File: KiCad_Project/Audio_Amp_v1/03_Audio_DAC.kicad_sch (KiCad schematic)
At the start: 0 parts

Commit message: Updated Power management section, Bluetooth receiver and connectors. Added some components footprints and 3D.
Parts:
- added U1: PCM2704CDB, PCM2704CDB:SOP65P780X200-28N, symbol PCM2704CDB:PCM2704CDB
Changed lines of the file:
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@@
 	(generator_version "9.0")
 	(paper "A4")
+	(symbol
+		(lib_id "PCM2704CDB:PCM2704CDB")
+		(at 134.62 97.79 0)
+		(unit 1)
+		(exclude_from_sim no)
+		(in_bom yes)
+		(on_board yes)
+		(dnp no)
+		(fields_autoplaced yes)
+		(property "Reference" "U1"
+			(at 134.62 57.15 0)
+			(effects
+				(font
+					(size 1.27 1.27)
+				)
+			)
+		)
+		(property "Value" "PCM2704CDB"
+			(at 134.62 59.69 0)
+			(effects
+				(font
+					(size 1.27 1.27)
+				)
+			)
+		)
+		(property "Footprint" "PCM2704CDB:SOP65P780X200-28N"
+			(at 134.62 97.79 0)
+			(effects
+				(font
+					(size 1.27 1.27)
+				)
+				(justify bottom)
+				(hide yes)
+			)
+		)
+		(property "Datasheet" "kicad-embed://pcm2704c.pdf"
+			(at 134.62 97.79 0)
+			(effects
+				(font
+					(size 1.27 1.27)
+				)
+				(hide yes)
+			)
+		)
+		(property "Description" "IC DAS/ADC/DAC SPECIAL 28-SSOP"
+			(at 134.62 97.79 0)
+			(effects
+				(font
+					(size 1.27 1.27)
+				)
+				(hide yes)
+			)
+		)
+		(pin "28"
+		)
+		(pin "4"
+		)
+		(pin "3"
+		)
+		(pin "21"
+		)
+		(pin "18"
+		)
+		(pin "23"
+		)
+		(pin "5"
+		)
+		(pin "7"
+		)
+		(pin "10"
+		)
+		(pin "20"
+		)
+		(pin "26"
+		)
+		(pin "22"
+		)
+		(pin "14"
+		)
+		(pin "15"
+		)
+		(pin "11"
+		)
+		(pin "24"
+		)
+		(pin "9"
+		)
+		(pin "25"
+		)
+		(pin "8"
+		)
+		(pin "13"
+		)
+		(pin "16"
+		)
+		(pin "27"
+		)
+		(pin "6"
+		)
+		(pin "1"
+		)
+		(pin "2"
+		)
+		(pin "12"
+		)
+		(pin "17"
+		)
+		(pin "19"
+		)
+		(instances
+			(project ""
+				(path "/d992164b-b1d0-4285-be2c-12a40c17e5cc/b3acd54a-fc58-4bfe-bc83-94fecc26a81e"
+					(reference "U1")
+					(unit 1)
+				)
+			)
+		)
+	)
 )

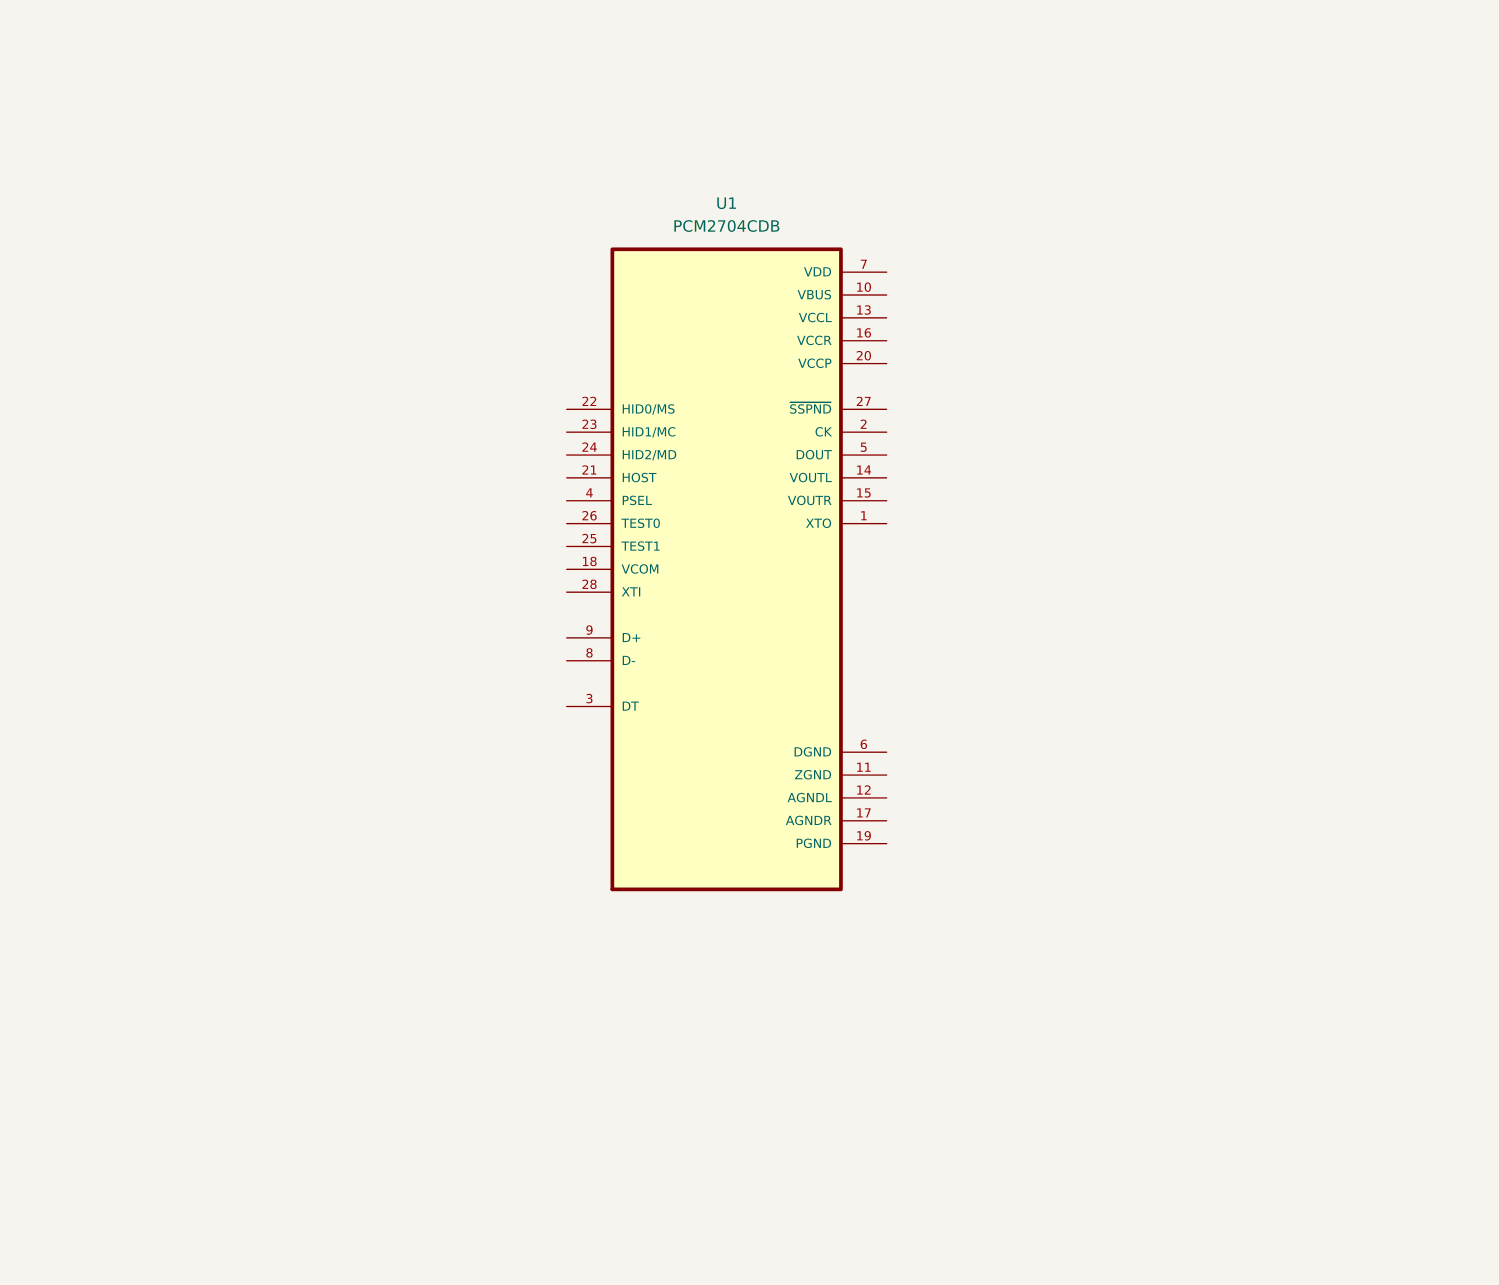
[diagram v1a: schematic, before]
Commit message: Added USB_C schematic and updated the DAC
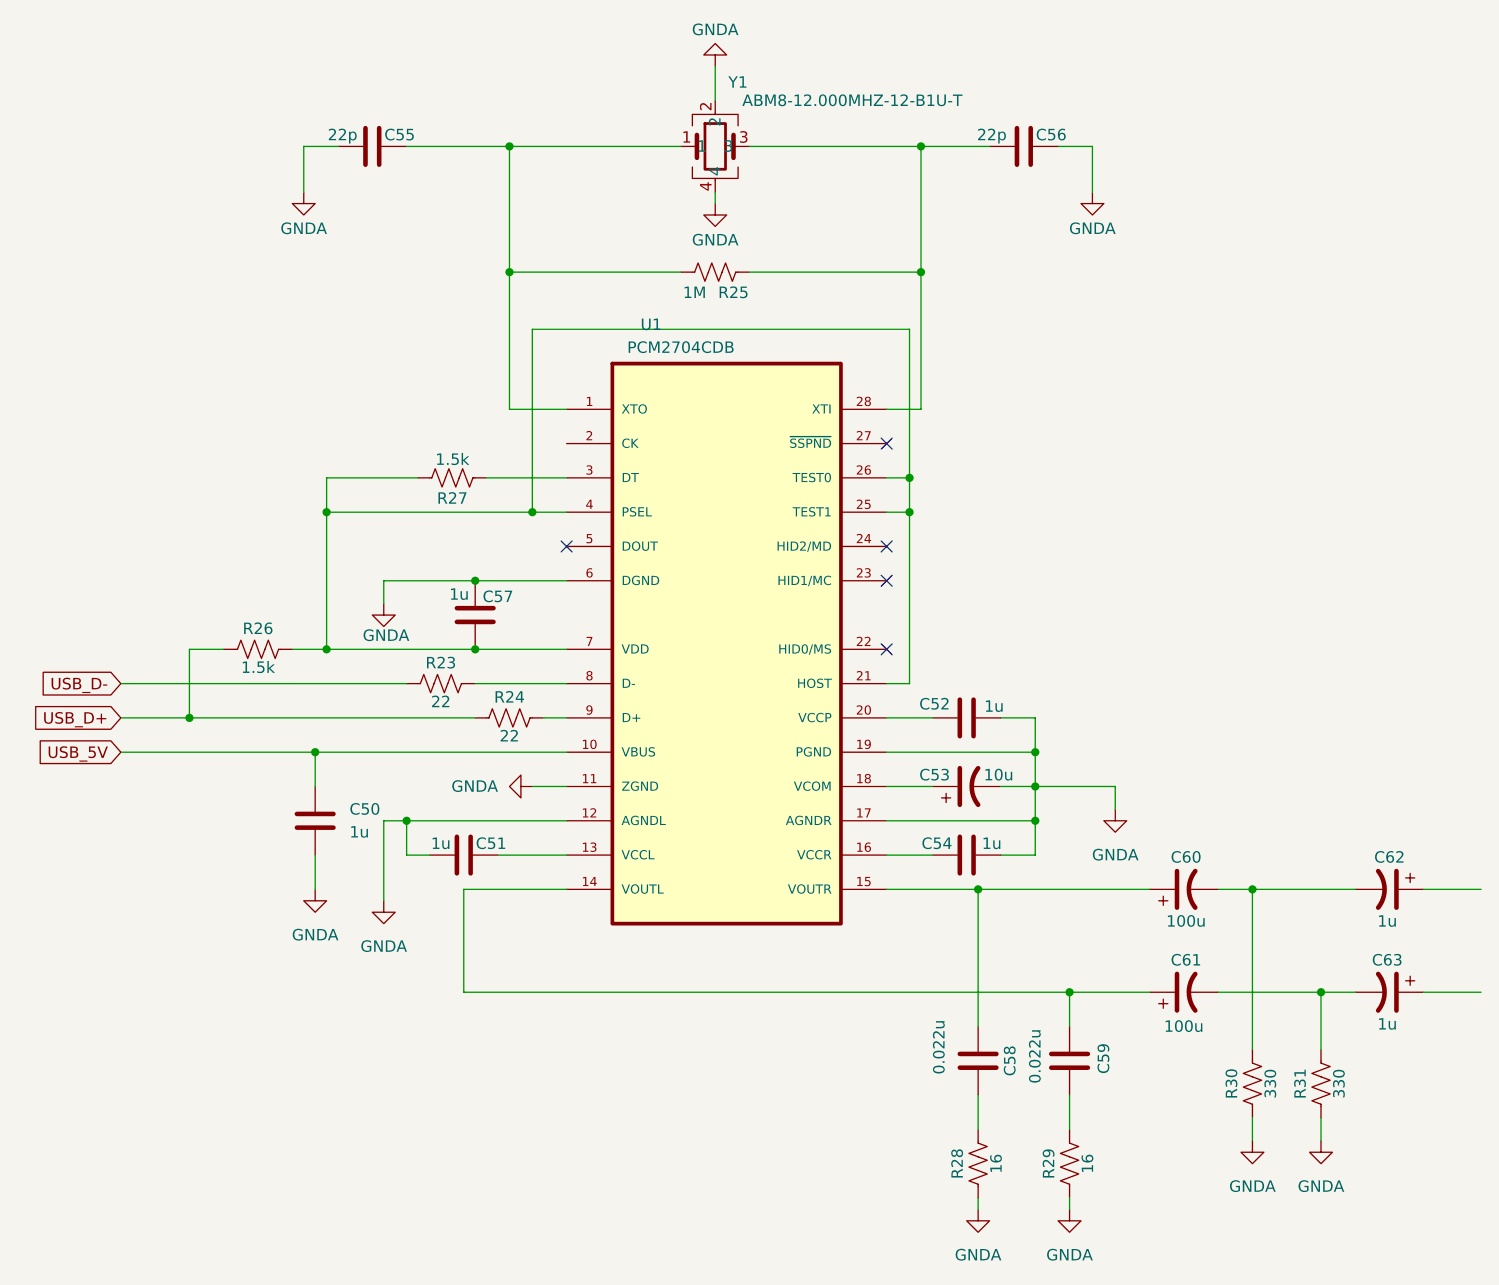
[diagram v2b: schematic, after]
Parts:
- added C50, C51, C52, C54, C57: 1u, symbol Device:C
- added C53: 10u, symbol Device:C_Polarized_US
- added C55, C56: 22p, symbol Device:C
- added C58, C59: 0.022u, symbol Device:C
- added C60, C61: 100u, symbol Device:C_Polarized_US
- added C62, C63: 1u, symbol Device:C_Polarized_US
- added R23, R24: 22, symbol Device:R_US
- added R25: 1M, symbol Device:R_US
- added R26, R27: 1.5k, symbol Device:R_US
- added R28, R29: 16, symbol Device:R_US
- added R30, R31: 330, symbol Device:R_US
- added Y1: ABM8-12.000MHZ-12-B1U-T, ABM810000MHZ12D2W, symbol ABM8-12_000MHZ-12-B1U-T:ABM8-12.000MHZ-12-B1U-T
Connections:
- net at U1.1 (XTO): now also C55.2, R25.1, Y1.1
- net USB_5V: now reaches U1.10 (VBUS)
- net USB_5V: now also C50.1
- net GNDA: now reaches U1.11 (ZGND)
- net GNDA: now also U1.12 (AGNDL), U1.17 (AGNDR), U1.19 (PGND), U1.6 (DGND), C50.2, C51.1, C52.2, C53.2, C54.2, C55.1, C56.2, C57.2, R28.1, R29.1, R30.1, R31.1, Y1.2, Y1.4
- net at U1.13 (VCCL): now also C51.2
- net at U1.14 (VOUTL): now also C59.2, C61.1
- net at U1.15 (VOUTR): now also C58.2, C60.1
- net at U1.16 (VCCR): now also C54.1
- net at U1.18 (VCOM): now also C53.1
- net at U1.20 (VCCP): now also C52.1
- net at U1.21 (HOST): now also U1.25 (TEST1), U1.26 (TEST0), U1.4 (PSEL), U1.7 (VDD), C57.1, R26.2, R27.2
- net at U1.28 (XTI): now also C56.1, R25.2, Y1.3
- net at U1.3 (DT): now also R27.1
- net at U1.8 (D-): now also R23.2
- net at U1.9 (D+): now also R24.2
- new net: C61.2, C63.2, R31.2
- new net: C58.1, R28.2
- new net: C59.1, R29.2
- new net: C60.2, C62.2, R30.2
- new net USB_D+: R24.1, R26.1
- new net USB_D-: R23.1
- no-connect marks 0 -> 5
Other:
- moved on the sheet: U1
